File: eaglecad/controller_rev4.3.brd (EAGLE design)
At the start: 40 x 29.5 mm, 79 parts, among them U100 STM32L452XX_QFPN48, U101 TCAN330, U200 TPS63070, U300 STSPIN230, U301 TSV991ILT, U302 AS5047P, U400 STSPIN250, U401 TSV991ILT, X101 ABM10-16MHz

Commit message: minor modifications
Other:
- board text added: "ACS Driver OreSat Rev 4.3 Eric Ruhl"
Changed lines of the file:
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@@
 <?xml version="1.0" encoding="utf-8"?>
 <!DOCTYPE eagle SYSTEM "eagle.dtd">
-<eagle version="9.5.1">
+<eagle version="9.4.2">
 <drawing>
 <settings>
-<setting alwaysvectorfont="no"/>
+<setting alwaysvectorfont="yes"/>
 <setting verticaltext="up"/>
 </settings>
@@
 <layer number="14" name="Route14" color="1" fill="6" visible="no" active="no"/>
 <layer number="15" name="Route15" color="16" fill="1" visible="no" active="yes"/>
-<layer number="16" name="Bottom" color="38" fill="1" visible="no" active="yes"/>
+<layer number="16" name="Bottom" color="38" fill="1" visible="yes" active="yes"/>
 <layer number="17" name="Pads" color="2" fill="1" visible="yes" active="yes"/>
 <layer number="18" name="Vias" color="2" fill="1" visible="yes" active="yes"/>
@@
 <layer number="22" name="bPlace" color="7" fill="1" visible="no" active="yes"/>
 <layer number="23" name="tOrigins" color="15" fill="1" visible="yes" active="yes"/>
-<layer number="24" name="bOrigins" color="15" fill="1" visible="no" active="yes"/>
+<layer number="24" name="bOrigins" color="15" fill="1" visible="yes" active="yes"/>
 <layer number="25" name="tNames" color="7" fill="1" visible="no" active="yes"/>
 <layer number="26" name="bNames" color="7" fill="1" visible="no" active="yes"/>
@@
 <circle x="13.82" y="21.53" radius="0.111803125" width="0.25" layer="29"/>
 <circle x="14.822" y="22.02" radius="0.107703125" width="0.25" layer="29"/>
-<circle x="15.08" y="21.01" radius="0.1063" width="0.25" layer="29"/>
+<circle x="14.35" y="21.05" radius="0.1063" width="0.25" layer="29"/>
 <circle x="14.4" y="23.17" radius="0.1063" width="0.25" layer="29"/>
 <rectangle x1="14" y1="23.63" x2="14.26" y2="23.89" layer="29"/>
@@
 <rectangle x1="14" y1="20.27" x2="14.26" y2="20.53" layer="29"/>
 <rectangle x1="14" y1="19.7" x2="14.26" y2="19.96" layer="29"/>
-<text x="14.67" y="15.52" size="1" layer="21" font="vector" ratio="10">ACS Driver
+<text x="14.67" y="14.02" size="1" layer="21" font="vector" ratio="10">ACS Driver
 OreSat
-Rev 4.2B
+Rev 4.3
 Eric Ruhl</text>
 </plain>
@@
 <via x="5.91" y="7.48" extent="1-16" drill="0.254"/>
 <via x="7.72" y="7.39" extent="1-16" drill="0.254"/>
-<via x="18.72" y="16.25" extent="1-16" drill="0.254"/>
-<via x="17.94" y="13.85" extent="1-16" drill="0.254"/>
-<via x="15.09" y="14.15" extent="1-16" drill="0.254"/>
+<via x="18.33" y="16.47" extent="1-16" drill="0.254"/>
+<via x="17.5" y="13.5" extent="1-16" drill="0.254"/>
+<via x="15" y="13.04" extent="1-16" drill="0.254"/>
 <via x="2" y="17" extent="1-16" drill="0.254"/>
 <via x="2" y="27" extent="1-16" drill="0.254"/>
@@
 <via x="32" y="6" extent="1-16" drill="0.254"/>
 <via x="36.88" y="14.8" extent="1-16" drill="0.254"/>
-<via x="16" y="17" extent="1-16" drill="0.254"/>
+<via x="16.02" y="16.78" extent="1-16" drill="0.254"/>
 <via x="15.91" y="23.04" extent="1-16" drill="0.254"/>
 <contactref element="C104" pad="2"/>
@@
 <wire x1="20" y1="15.195" x2="20" y2="14.58" width="0.25" layer="16"/>
 <wire x1="20" y1="14.58" x2="19.72" y2="14.3" width="0.25" layer="16"/>
-<via x="20.61" y="13.82" extent="1-16" drill="0.254"/>
+<via x="21" y="14" extent="1-16" drill="0.254"/>
 <via x="20.85" y="23" extent="1-16" drill="0.254"/>
 <via x="23.55" y="22.23" extent="1-16" drill="0.254"/>
@@
 <vertex x="12.387059375" y="7.012940625"/>
 </polygon>
-<wire x1="19.72" y1="13.83" x2="20.61" y2="13.82" width="0.254" layer="16"/>
+<wire x1="21" y1="14" x2="19.902334375" y2="14.012334375" width="0.254" layer="16"/>
+<wire x1="19.72" y1="13.83" x2="19.902334375" y2="14.012334375" width="0.254" layer="16"/>
 <via x="32.04" y="19.25" extent="1-16" drill="0.254"/>
 <via x="11.59" y="10.29" extent="1-16" drill="0.254"/>
@@
 <contactref element="U400" pad="14"/>
 <wire x1="28.25" y1="14.625" x2="28.25" y2="13.6607875" width="0.254" layer="1"/>
-<wire x1="28.25" y1="13.6607875" x2="26.1342125" y2="11.545" width="0.254" layer="1"/>
+<wire x1="28.25" y1="13.6607875" x2="26.54460625" y2="11.95539375" width="0.254" layer="1"/>
+<wire x1="26.54460625" y1="11.95539375" x2="26.1342125" y2="11.545" width="0.254" layer="1"/>
 <wire x1="26.1342125" y1="11.545" x2="25.8" y2="11.545" width="0.254" layer="1"/>
 <wire x1="25.8" y1="11.545" x2="25.8" y2="11.53" width="0.254" layer="1"/>
@@
 <contactref element="U$2" pad="P$22"/>
 <wire x1="27.26" y1="11.73" x2="24.8425" y2="11.73" width="0.254" layer="16"/>
-<wire x1="24.8425" y1="11.73" x2="22.0789" y2="8.9664" width="0.254" layer="16"/>
-<wire x1="22.0789" y1="8.9664" x2="18.918775" y2="8.9664" width="0.254" layer="16"/>
-<via x="18.918775" y="8.9664" extent="1-16" drill="0.254"/>
-<wire x1="18.918775" y1="8.9664" x2="18.778775" y2="8.9664" width="0.254" layer="1"/>
-<wire x1="18.778775" y1="8.9664" x2="17.8" y2="7.987625" width="0.254" layer="1"/>
-<wire x1="17.8" y1="7.987625" x2="17.8" y2="7.3" width="0.254" layer="1"/>
+<wire x1="22.0789" y1="8.9664" x2="24.8425" y2="11.73" width="0.254" layer="16"/>
 <wire x1="17.8" y1="7.3" x2="17.8" y2="3.3" width="0.254" layer="1"/>
+<via x="17.8" y="8.52" extent="1-16" drill="0.254"/>
+<wire x1="17.8" y1="8.52" x2="18.2464" y2="8.9664" width="0.254" layer="16"/>
+<wire x1="17.8" y1="7.3" x2="17.8" y2="8.52" width="0.254" layer="1"/>
+<wire x1="18.2464" y1="8.9664" x2="22.0789" y2="8.9664" width="0.254" layer="16"/>
 </signal>
 <signal name="B_IN+">
@@
 <wire x1="21.5926" y1="11.8133875" x2="21.5926" y2="10.9801" width="0.254" layer="16"/>
 <wire x1="21.5926" y1="10.9801" x2="20.4425" y2="9.83" width="0.254" layer="16"/>
-<wire x1="20.4425" y1="9.83" x2="18.13" y2="9.83" width="0.254" layer="16"/>
-<via x="18.13" y="9.83" extent="1-16" drill="0.254"/>
-<wire x1="18.13" y1="9.83" x2="16.8" y2="8.5" width="0.254" layer="1"/>
-<wire x1="16.8" y1="8.5" x2="16.8" y2="7.3" width="0.254" layer="1"/>
 <wire x1="16.8" y1="7.3" x2="16.8" y2="3.3" width="0.254" layer="1"/>
+<wire x1="17.42" y1="9.83" x2="16.88" y2="9.29" width="0.254" layer="16"/>
+<via x="16.88" y="9.29" extent="1-16" drill="0.254"/>
+<wire x1="16.88" y1="9.29" x2="16.8" y2="9.21" width="0.254" layer="1"/>
+<wire x1="20.4425" y1="9.83" x2="17.42" y2="9.83" width="0.254" layer="16"/>
+<wire x1="16.8" y1="9.21" x2="16.8" y2="7.3" width="0.254" layer="1"/>
 </signal>
 <signal name="I2C_SDA">
@@
 <contactref element="U$2" pad="P$23"/>
 <contactref element="U$2" pad="P$8"/>
-<wire x1="21.9736" y1="10.82228125" x2="20.60031875" y2="9.449" width="0.254" layer="16"/>
 <wire x1="23.5118" y1="13.1743" x2="21.9736" y2="11.6361" width="0.254" layer="16"/>
 <wire x1="21.9736" y1="11.6361" x2="21.9736" y2="10.82228125" width="0.254" layer="16"/>
-<wire x1="20.60031875" y1="9.449" x2="18.5751875" y2="9.449" width="0.254" layer="16"/>
-<wire x1="18.5751875" y1="9.449" x2="18.4735875" y2="9.3474" width="0.254" layer="16"/>
-<via x="18.4735875" y="9.3474" extent="1-16" drill="0.254"/>
-<wire x1="18.4735875" y1="9.3474" x2="17.3" y2="8.1738125" width="0.254" layer="1"/>
-<wire x1="17.3" y1="8.1738125" x2="17.3" y2="7.3" width="0.254" layer="1"/>
-<wire x1="17.3" y1="7.3" x2="17.3" y2="5.4" width="0.254" layer="1"/>
-<wire x1="17.3" y1="5.4" x2="17.3" y2="3.3" width="0.254" layer="1"/>
-<wire x1="17.3" y1="5.4" x2="17.3" y2="5.4" width="0.254" layer="1"/>
+<wire x1="17.3" y1="8.1738125" x2="17.3" y2="8" width="0.254" layer="1"/>
+<wire x1="17.3" y1="8" x2="17.3" y2="7.3" width="0.254" layer="1"/>
+<wire x1="17.3" y1="7.3" x2="17.3" y2="3.3" width="0.254" layer="1"/>
+<via x="17.3026" y="8.8564125" extent="1-16" drill="0.254"/>
+<wire x1="17.84095625" y1="9.4074" x2="20.55871875" y2="9.4074" width="0.254" layer="16"/>
+<wire x1="21.9736" y1="10.82228125" x2="20.55871875" y2="9.4074" width="0.254" layer="16"/>
+<wire x1="17.3026" y1="8.8564125" x2="17.3026" y2="8.86904375" width="0.254" layer="16"/>
+<wire x1="17.3026" y1="8.86904375" x2="17.84095625" y2="9.4074" width="0.254" layer="16"/>
+<wire x1="17.3" y1="8.1738125" x2="17.3" y2="8.8538125" width="0.254" layer="1"/>
+<wire x1="17.3" y1="8.8538125" x2="17.3026" y2="8.8564125" width="0.254" layer="1"/>
 </signal>
 <signal name="ADDR_0">

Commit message: Flattening the board
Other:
- board text removed: "ACS Driver OreSat Rev 4.2B Eric Ruhl"
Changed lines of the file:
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@@
 <layer number="20" name="Dimension" color="24" fill="1" visible="yes" active="yes"/>
 <layer number="21" name="tPlace" color="7" fill="1" visible="yes" active="yes"/>
-<layer number="22" name="bPlace" color="7" fill="1" visible="no" active="yes"/>
+<layer number="22" name="bPlace" color="7" fill="1" visible="yes" active="yes"/>
 <layer number="23" name="tOrigins" color="15" fill="1" visible="yes" active="yes"/>
 <layer number="24" name="bOrigins" color="15" fill="1" visible="yes" active="yes"/>
@@
 <circle x="33.5" y="4.5" radius="2.5" width="0.1524" layer="39"/>
 <circle x="33.5" y="27.5" radius="2.5" width="0.1524" layer="39"/>
-<text x="17.83" y="8.02" size="1" layer="22" font="vector" ratio="10" rot="MR0">ACS Driver
-OreSat
-Rev 4.2B
-Eric Ruhl</text>
 <rectangle x1="24.5" y1="25.5" x2="32" y2="29.5" layer="21"/>
 <rectangle x1="23.18" y1="20.12" x2="23.45" y2="20.38" layer="29"/>

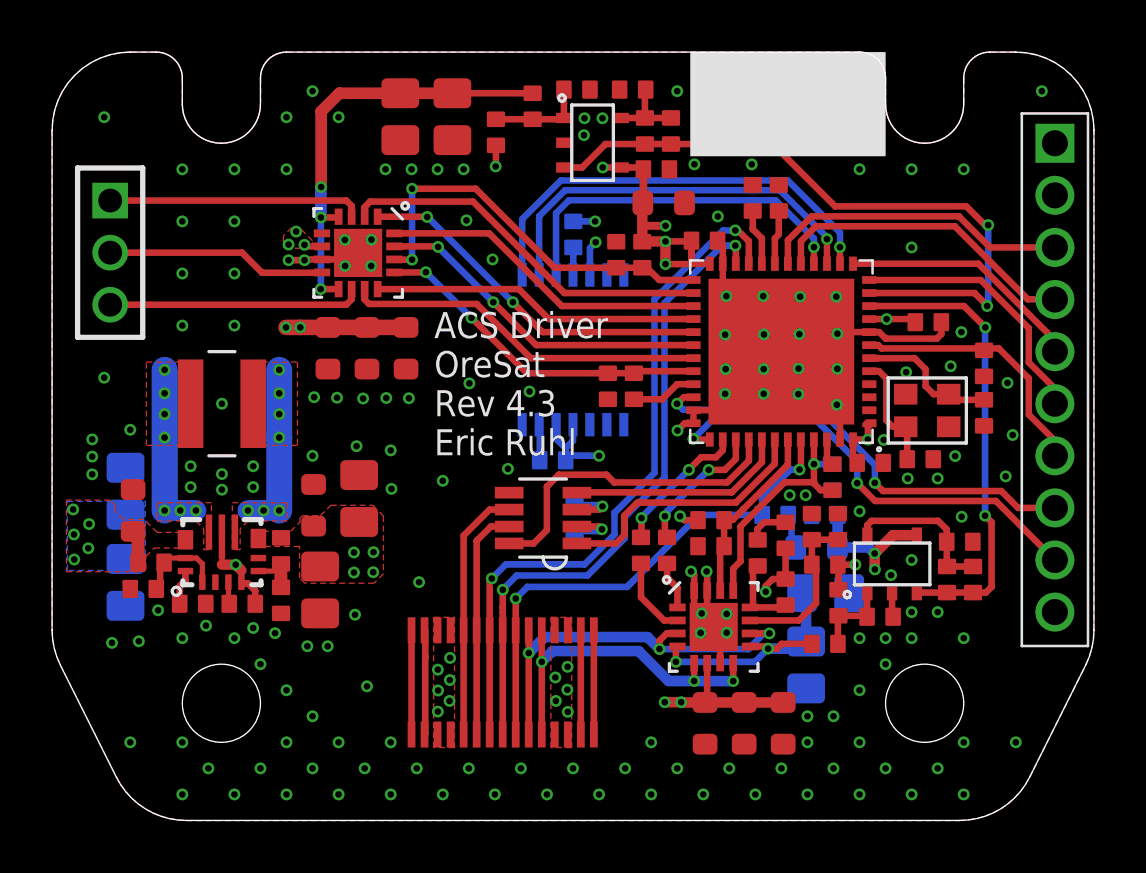
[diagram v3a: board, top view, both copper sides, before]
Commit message: test point updates to rev4.3, DRC approval for flat rev4.3
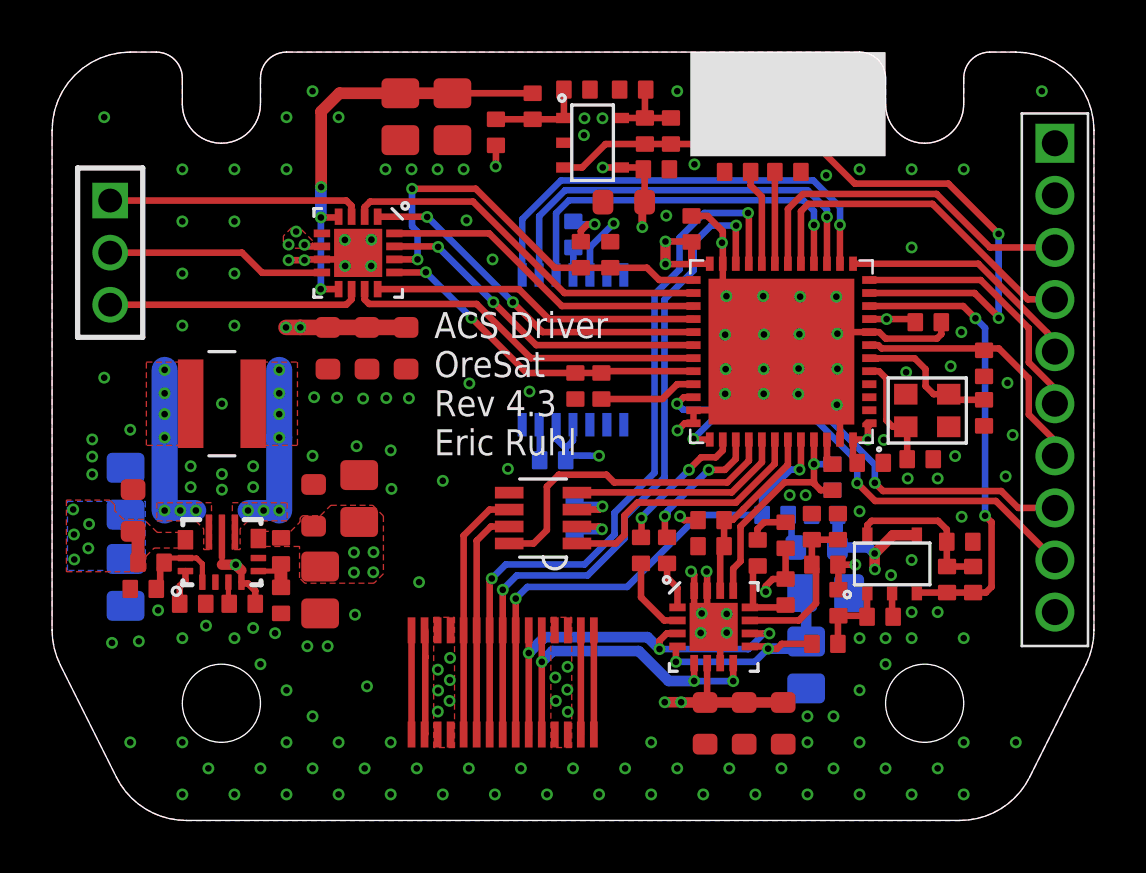
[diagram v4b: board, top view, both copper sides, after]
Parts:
- moved R301 2.36 mm to (20.3, 21.7)
- moved C306 1.53 mm to (21.9, 23.7), turned to 180 degrees
- moved C305 1.25 mm to (20.1, 16.7)
- moved R302 1.25 mm to (21.1, 16.7)
- moved R103 1.16 mm to (26.3, 24.9), turned to 0 degrees
- moved R102 1.06 mm to (28.2, 24.9), turned to 180 degrees
- moved C102 0.67 mm to (24.6, 22.7), turned to 90 degrees
- moved C304 0.23 mm to (21.4, 21.7)
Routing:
- net GND: track 60.2 -> 62.9 mm, vias 179 -> 180
- net I2C_SCL: track 26.9 -> 28.9 mm
- net I2C_SDA: track 25.1 -> 26.9 mm
- net ADDR_1: track 2.17 -> 3.70 mm
- net ADDR_0: track 2.09 -> 3.52 mm
- net DEBUG_1: track 12.0 -> 13.4 mm
- net DEBUG_2: track 12.0 -> 13.4 mm
- net BLDC_CURR_FDB: track 25.8 -> 27.1 mm
- net BLDC_EN: track 2.53 -> 3.77 mm
- net 3.3V: track 31.0 -> 29.8 mm
- net SPI1_SCK: track 15.5 -> 16.1 mm
- net SPI1_MISO: track 14.1 -> 14.7 mm
- net SPI1_CS: track 17.0 -> 17.6 mm
